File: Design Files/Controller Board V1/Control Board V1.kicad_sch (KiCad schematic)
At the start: 1 part, among them U1 MIC29752WWT

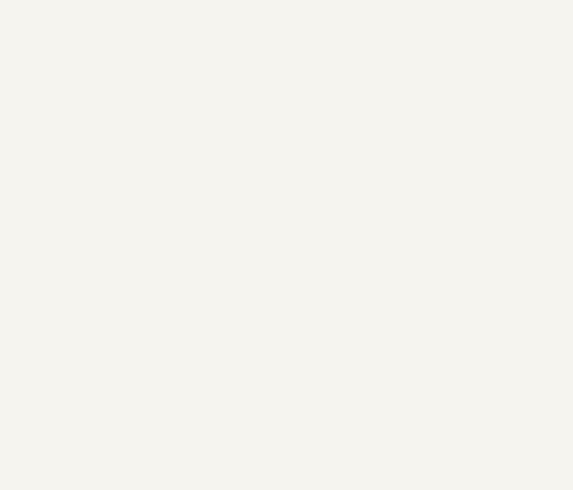
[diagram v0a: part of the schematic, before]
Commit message: Added LM chip for 5V supply
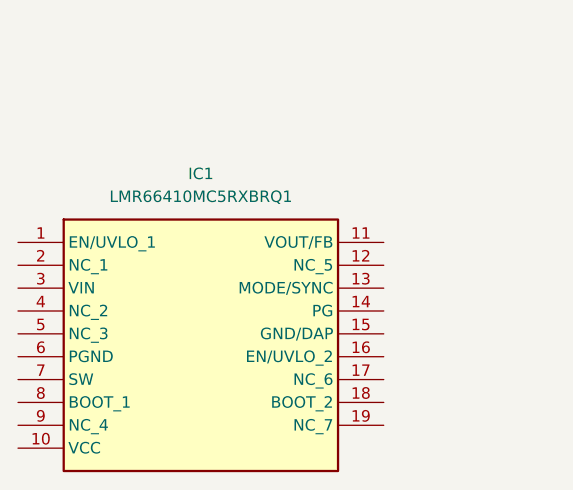
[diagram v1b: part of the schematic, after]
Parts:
- added IC1: LMR66410MC5RXBRQ1, LMR66430R5RXBR, symbol LMR66410MC5RXBRQ1:LMR66410MC5RXBRQ1
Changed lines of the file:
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@@
+		)
+	)
+	(symbol
+		(lib_id "LMR66410MC5RXBRQ1:LMR66410MC5RXBRQ1")
+		(at 83.82 128.27 0)
+		(unit 1)
+		(exclude_from_sim no)
+		(in_bom yes)
+		(on_board yes)
+		(dnp no)
+		(fields_autoplaced yes)
+		(property "Reference" "IC1"
+			(at 104.14 120.65 0)
+			(effects
+				(font
+					(size 1.27 1.27)
+				)
+			)
+		)
+		(property "Value" "LMR66410MC5RXBRQ1"
+			(at 104.14 123.19 0)
+			(effects
+				(font
+					(size 1.27 1.27)
+				)
+			)
+		)
+		(property "Footprint" "LMR66430R5RXBR"
+			(at 120.65 223.19 0)
+			(effects
+				(font
+					(size 1.27 1.27)
+				)
+				(justify left top)
+				(hide yes)
+			)
+		)
+		(property "Datasheet" "https://www.ti.com/lit/ds/symlink/lmr66410-q1.pdf?ts=1721818426911&ref_url=https%253A%252F%252Fwww.ti.com%252Fproduct%252FLMR66410-Q1%252Fpart-details%252FLMR66410MC5RXBRQ1%253Futm_source%253Dgoogle%2526utm_medium%253Dcpc%2526utm_campaign%253Docb-tistore-"
+			(at 120.65 323.19 0)
+			(effects
+				(font
+					(size 1.27 1.27)
+				)
+				(justify left top)
+				(hide yes)
+			)
+		)
+		(property "Description" "Switching Voltage Regulators Automotive, 36V, 1A synchronous step-down converter with 1.5uA IQ and low EMI 14-VQFN-FCRLF -40 to 125"
+			(at 83.82 128.27 0)
+			(effects
+				(font
+					(size 1.27 1.27)
+				)
+				(hide yes)
+			)
+		)
+		(property "Height" "1.05"
+			(at 120.65 523.19 0)
+			(effects
+				(font
+					(size 1.27 1.27)
+				)
+				(justify left top)
+				(hide yes)
+			)
+		)
+		(property "Mouser Part Number" "595-LMR66410MC5RXRQ1"
+			(at 120.65 623.19 0)
+			(effects
+				(font
+					(size 1.27 1.27)
+				)
+				(justify left top)
+				(hide yes)
+			)
+		)
+		(property "Mouser Price/Stock" "https://www.mouser.co.uk/ProductDetail/Texas-Instruments/LMR66410MC5RXBRQ1?qs=ZcfC38r4Posa4PoE3lfIOA%3D%3D"
+			(at 120.65 723.19 0)
+			(effects
+				(font
+					(size 1.27 1.27)
+				)
+				(justify left top)
+				(hide yes)
+			)
+		)
+		(property "Manufacturer_Name" "Texas Instruments"
+			(at 120.65 823.19 0)
+			(effects
+				(font
+					(size 1.27 1.27)
+				)
+				(justify left top)
+				(hide yes)
+			)
+		)
+		(property "Manufacturer_Part_Number" "LMR66410MC5RXBRQ1"
+			(at 120.65 923.19 0)
+			(effects
+				(font
+					(size 1.27 1.27)
+				)
+				(justify left top)
+				(hide yes)
+			)
+		)
+		(pin "1"
+		)
+		(pin "8"
+		)
+		(pin "7"
+		)
+		(pin "13"
+		)
+		(pin "15"
+		)
+		(pin "3"
+		)
+		(pin "16"
+		)
+		(pin "9"
+		)
+		(pin "17"
+		)
+		(pin "18"
+		)
+		(pin "19"
+		)
+		(pin "14"
+		)
+		(pin "5"
+		)
+		(pin "10"
+		)
+		(pin "11"
+		)
+		(pin "12"
+		)
+		(pin "4"
+		)
+		(pin "6"
+		)
+		(pin "2"
+		)
+		(instances
+			(project ""
+				(path "/e0c606b8-cbb9-4aff-b96c-73876da6ca74"
+					(reference "IC1")
+					(unit 1)
+				)
+			)
 		)
 	)

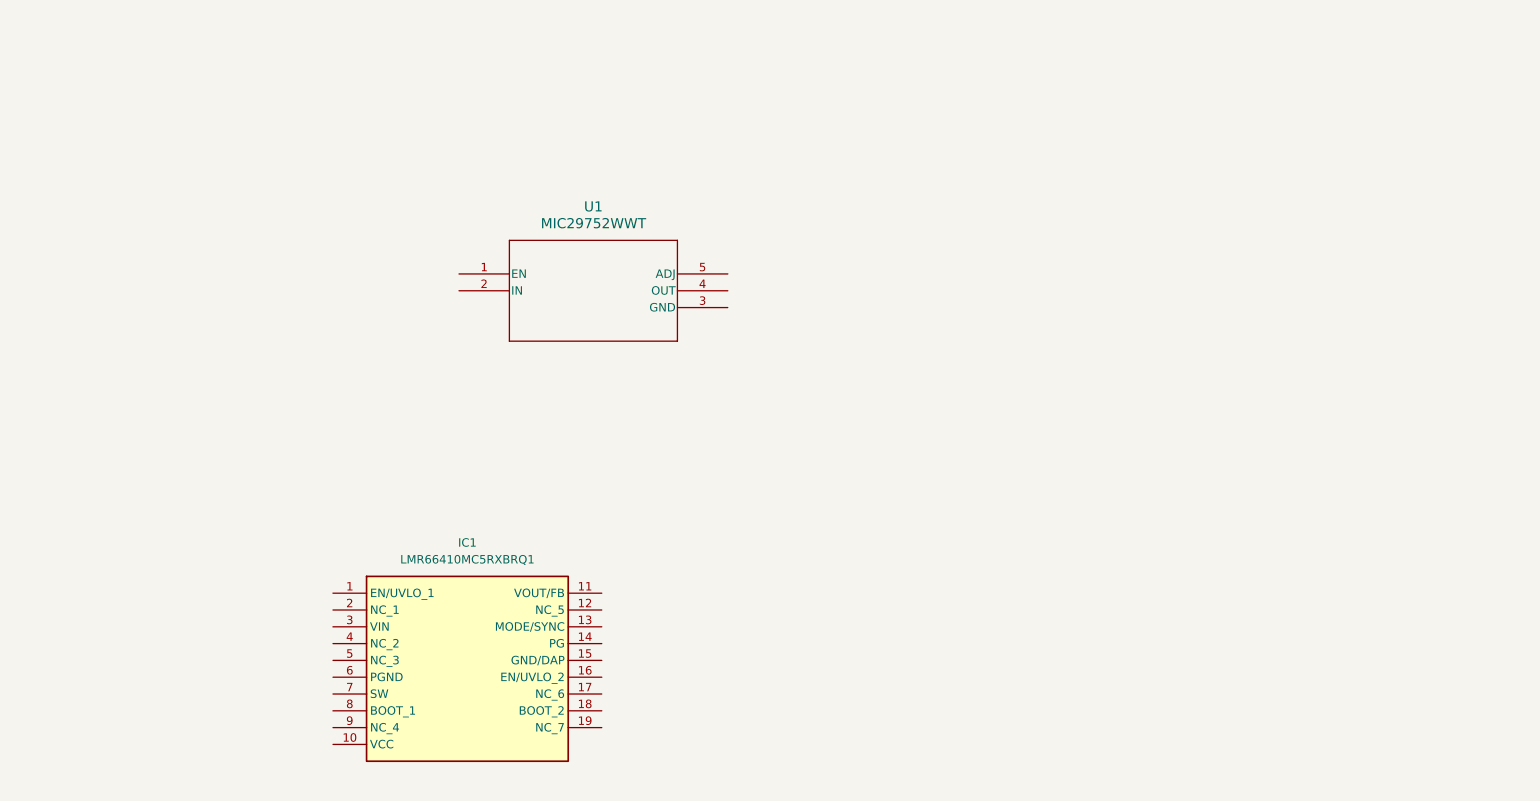
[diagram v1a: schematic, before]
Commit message: Power Supply Board For Pico
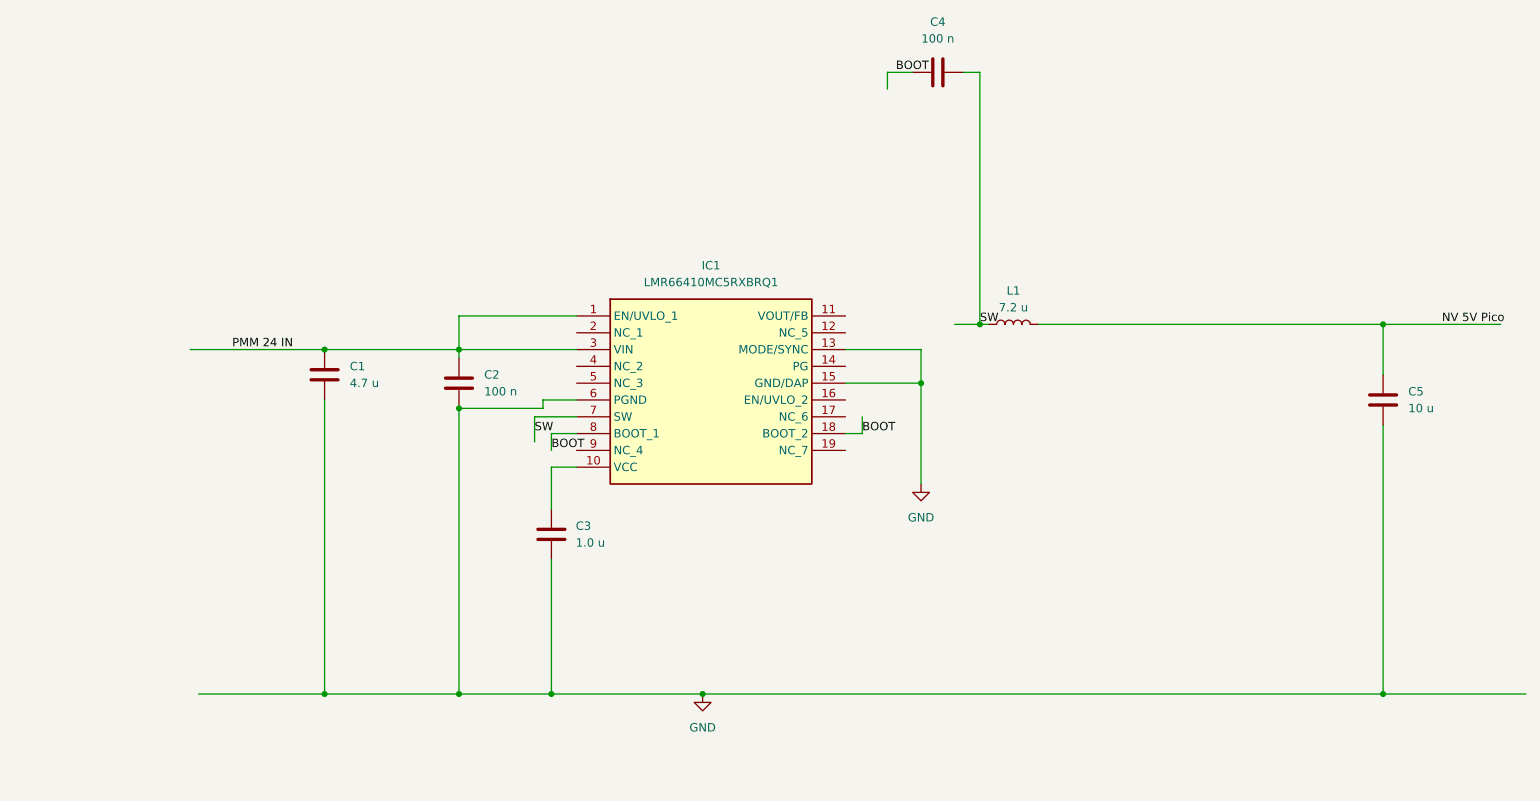
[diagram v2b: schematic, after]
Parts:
- removed U1: MIC29752WWT, MIC29752WWT:TO-247-5_MCH, symbol MIC2975WWT:MIC29752WWT
- added C1: 4.7 u, symbol Device:C
- added C2, C4: 100 n, symbol Device:C
- added C3: 1.0 u, symbol Device:C
- added C5: 10 u, symbol Device:C
- added L1: 7.2 u, symbol Device:L
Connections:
- net PMM 24 IN: now reaches IC1.1 (EN/UVLO_1)
- net PMM 24 IN: now also IC1.3 (VIN), C1.2, C2.2
- net at IC1.10 (VCC): now also C3.2
- net GND: now reaches IC1.13 (MODE/SYNC)
- net GND: now also IC1.15 (GND/DAP), IC1.6 (PGND), C1.1, C2.1, C3.1, C5.1
- net BOOT: now reaches IC1.18 (BOOT_2)
- net BOOT: now also IC1.8 (BOOT_1), C4.2
- net SW: now reaches IC1.7 (SW)
- net SW: now also C4.1, L1.1
- new net NV 5V Pico: C5.2, L1.2
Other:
- moved on the sheet: IC1

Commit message: 5v
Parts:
- removed C1: 4.7 u, symbol Device:C
- removed C2, C4: 100 n, symbol Device:C
- removed C3: 1.0 u, symbol Device:C
- removed C5: 10 u, symbol Device:C
- removed IC1: LMR66410MC5RXBRQ1, LMR66430R5RXBR, symbol LMR66410MC5RXBRQ1:LMR66410MC5RXBRQ1
- removed L1: 7.2 u, symbol Device:L
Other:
- added sheet 5V_PSU (5V_PSU.kicad_sch)

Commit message: Made the THING
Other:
- sheet 5V_PSU ports: added GND, IOUT, VIN; removed none
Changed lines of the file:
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@@
+			)
+		)
+		(pin "IOUT" input
+			(at 109.22 57.912 180)
+			(effects
+				(font
+					(size 1.27 1.27)
+				)
+				(justify left)
+			)
+		)
+		(pin "GND" input
+			(at 109.22 60.96 180)
+			(effects
+				(font
+					(size 1.27 1.27)
+				)
+				(justify left)
+			)
+		)
+		(pin "VIN" input
+			(at 109.22 64.516 180)
+			(effects
+				(font
+					(size 1.27 1.27)
+				)
+				(justify left)
 			)
 		)

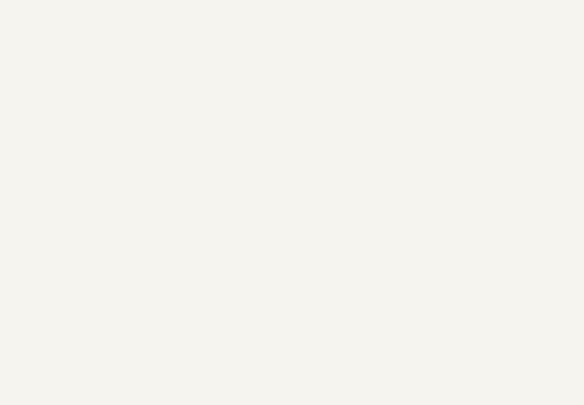
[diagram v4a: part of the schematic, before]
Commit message: Added male XT30s
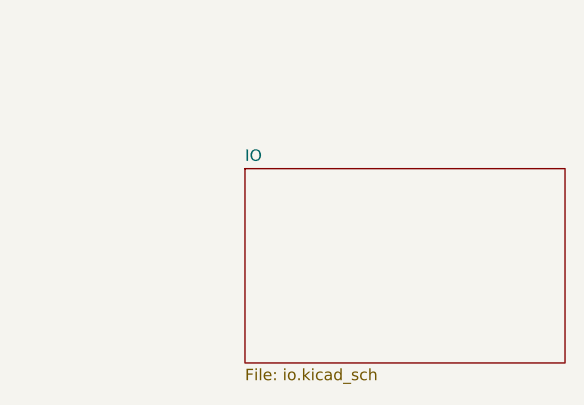
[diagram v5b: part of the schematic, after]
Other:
- added sheet IO (io.kicad_sch)
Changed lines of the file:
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@@
 	(paper "A4")
+	(sheet
+		(at 177.8 68.58)
+		(size 35.56 21.59)
+		(fields_autoplaced yes)
+		(stroke
+			(width 0.1524)
+			(type solid)
+		)
+		(fill
+			(color 0 0 0 0.0000)
+		)
+		(property "Sheetname" "IO"
+			(at 177.8 67.8684 0)
+			(effects
+				(font
+					(size 1.27 1.27)
+				)
+				(justify left bottom)
+			)
+		)
+		(property "Sheetfile" "io.kicad_sch"
+			(at 177.8 90.7546 0)
+			(effects
+				(font
+					(size 1.27 1.27)
+				)
+				(justify left top)
+			)
+		)
+		(instances
+			(project "Control Board V1"
+				(path "/e0c606b8-cbb9-4aff-b96c-73876da6ca74"
+					(page "3")
+				)
+			)
+		)
+	)
 	(sheet
 		(at 109.22 54.61)

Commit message: LMG5200 sheet i think
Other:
- added sheet LMG5200 (LMG5200.kicad_sch)
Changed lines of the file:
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@@
 	(paper "A4")
+	(sheet
+		(at 106.68 125.73)
+		(size 40.64 29.21)
+		(fields_autoplaced yes)
+		(stroke
+			(width 0.1524)
+			(type solid)
+		)
+		(fill
+			(color 0 0 0 0.0000)
+		)
+		(property "Sheetname" "LMG5200"
+			(at 106.68 125.0184 0)
+			(effects
+				(font
+					(size 1.27 1.27)
+				)
+				(justify left bottom)
+			)
+		)
+		(property "Sheetfile" "LMG5200.kicad_sch"
+			(at 106.68 155.5246 0)
+			(effects
+				(font
+					(size 1.27 1.27)
+				)
+				(justify left top)
+			)
+		)
+		(pin "sig-gnd" input
+			(at 147.32 146.05 0)
+			(effects
+				(font
+					(size 1.27 1.27)
+				)
+				(justify right)
+			)
+		)
+		(pin "5V" input
+			(at 135.89 125.73 90)
+			(effects
+				(font
+					(size 1.27 1.27)
+				)
+				(justify right)
+			)
+		)
+		(pin "bottom_out" input
+			(at 128.27 154.94 270)
+			(effects
+				(font
+					(size 1.27 1.27)
+				)
+				(justify left)
+			)
+		)
+		(pin "to_xt30_capBank" input
+			(at 106.68 137.16 180)
+			(effects
+				(font
+					(size 1.27 1.27)
+				)
+				(justify left)
+			)
+		)
+		(pin "ADC3" input
+			(at 113.03 125.73 90)
+			(effects
+				(font
+					(size 1.27 1.27)
+				)
+				(justify right)
+			)
+		)
+		(pin "ADC2" input
+			(at 116.84 125.73 90)
+			(effects
+				(font
+					(size 1.27 1.27)
+				)
+				(justify right)
+			)
+		)
+		(pin "PWM_top" input
+			(at 147.32 134.62 0)
+			(effects
+				(font
+					(size 1.27 1.27)
+				)
+				(justify right)
+			)
+		)
+		(pin "PWM_bottom" input
+			(at 147.32 137.16 0)
+			(effects
+				(font
+					(size 1.27 1.27)
+				)
+				(justify right)
+			)
+		)
+		(pin "ADC1" input
+			(at 120.65 125.73 90)
+			(effects
+				(font
+					(size 1.27 1.27)
+				)
+				(justify right)
+			)
+		)
+		(instances
+			(project "Control Board V1"
+				(path "/e0c606b8-cbb9-4aff-b96c-73876da6ca74"
+					(page "4")
+				)
+			)
+		)
+	)
 	(sheet
 		(at 177.8 68.58)

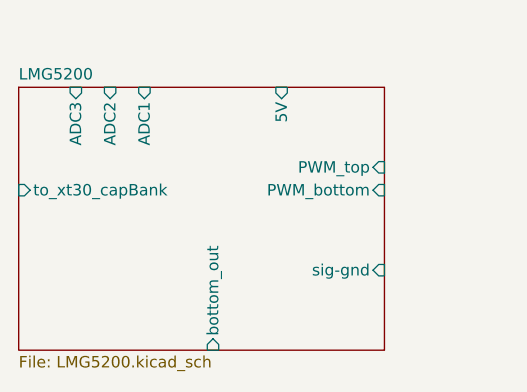
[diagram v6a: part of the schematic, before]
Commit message: small tweaks to half bridge schematic
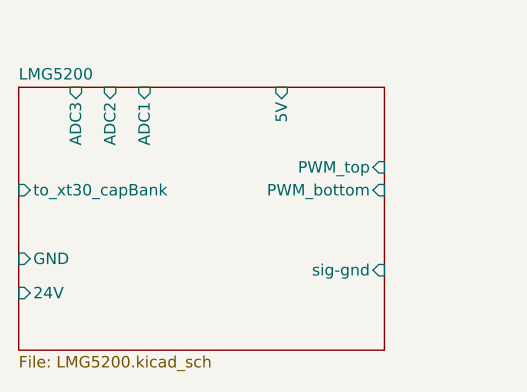
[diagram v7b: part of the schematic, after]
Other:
- sheet LMG5200 ports: added 24V, GND; removed bottom_out
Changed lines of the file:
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@@
-			)
-		)
-		(pin "bottom_out" input
-			(at 128.27 154.94 270)
-			(effects
-				(font
-					(size 1.27 1.27)
-				)
-				(justify left)
 			)
 		)
@@
 			)
 		)
+		(pin "GND" input
+			(at 106.68 144.78 180)
+			(effects
+				(font
+					(size 1.27 1.27)
+				)
+				(justify left)
+			)
+		)
+		(pin "24V" input
+			(at 106.68 148.59 180)
+			(effects
+				(font
+					(size 1.27 1.27)
+				)
+				(justify left)
+			)
+		)

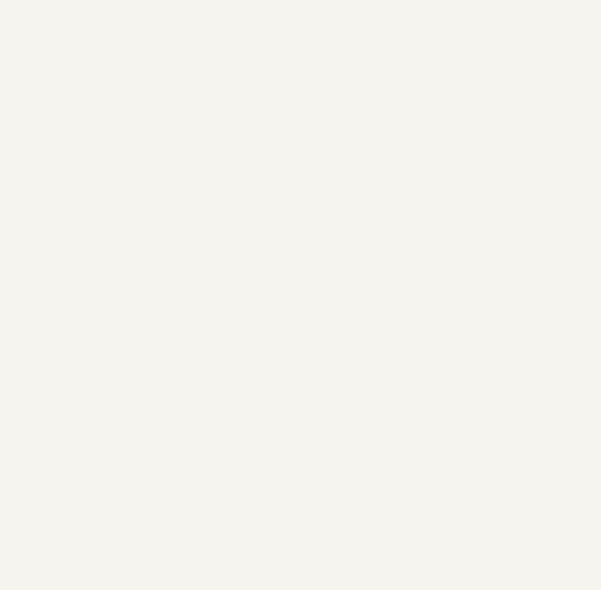
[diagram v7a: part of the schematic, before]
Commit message: added pico hierachical thing
might have messed up some pin names, pico schematic is not yet real, but we got the pins!!
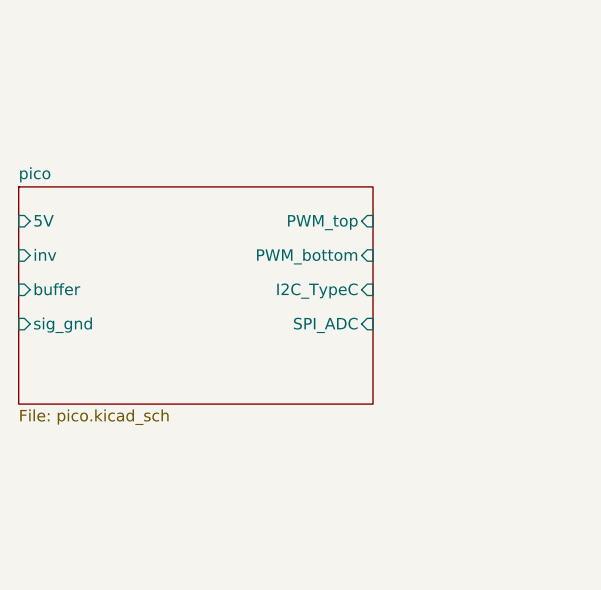
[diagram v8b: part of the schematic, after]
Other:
- added sheet pico (pico.kicad_sch)
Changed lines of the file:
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@@
+		)
+	)
+	(sheet
+		(at 35.56 96.52)
+		(size 39.37 24.13)
+		(fields_autoplaced yes)
+		(stroke
+			(width 0.1524)
+			(type solid)
+		)
+		(fill
+			(color 0 0 0 0.0000)
+		)
+		(property "Sheetname" "pico"
+			(at 35.56 95.8084 0)
+			(effects
+				(font
+					(size 1.27 1.27)
+				)
+				(justify left bottom)
+			)
+		)
+		(property "Sheetfile" "pico.kicad_sch"
+			(at 35.56 121.2346 0)
+			(effects
+				(font
+					(size 1.27 1.27)
+				)
+				(justify left top)
+			)
+		)
+		(pin "5V" input
+			(at 35.56 100.33 180)
+			(effects
+				(font
+					(size 1.27 1.27)
+				)
+				(justify left)
+			)
+		)
+		(pin "PWM_top" input
+			(at 74.93 100.33 0)
+			(effects
+				(font
+					(size 1.27 1.27)
+				)
+				(justify right)
+			)
+		)
+		(pin "PWM_bottom" input
+			(at 74.93 104.14 0)
+			(effects
+				(font
+					(size 1.27 1.27)
+				)
+				(justify right)
+			)
+		)
+		(pin "I2C_TypeC" input
+			(at 74.93 107.95 0)
+			(effects
+				(font
+					(size 1.27 1.27)
+				)
+				(justify right)
+			)
+		)
+		(pin "SPI_ADC" input
+			(at 74.93 111.76 0)
+			(effects
+				(font
+					(size 1.27 1.27)
+				)
+				(justify right)
+			)
+		)
+		(pin "sig_gnd" input
+			(at 35.56 111.76 180)
+			(effects
+				(font
+					(size 1.27 1.27)
+				)
+				(justify left)
+			)
+		)
+		(pin "inv" input
+			(at 35.56 104.14 180)
+			(effects
+				(font
+					(size 1.27 1.27)
+				)
+				(justify left)
+			)
+		)
+		(pin "buffer" input
+			(at 35.56 107.95 180)
+			(effects
+				(font
+					(size 1.27 1.27)
+				)
+				(justify left)
+			)
+		)
+		(instances
+			(project "Control Board V1"
+				(path "/e0c606b8-cbb9-4aff-b96c-73876da6ca74"
+					(page "5")
+				)
+			)
 		)
 	)
